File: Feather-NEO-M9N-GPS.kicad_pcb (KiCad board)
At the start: 2 copper layers, 50.8 x 22.9 mm, 43 parts, among them IC1 PRTR5V0U2F,115, J6 USB_B_Micro, U1 NEO-M9N

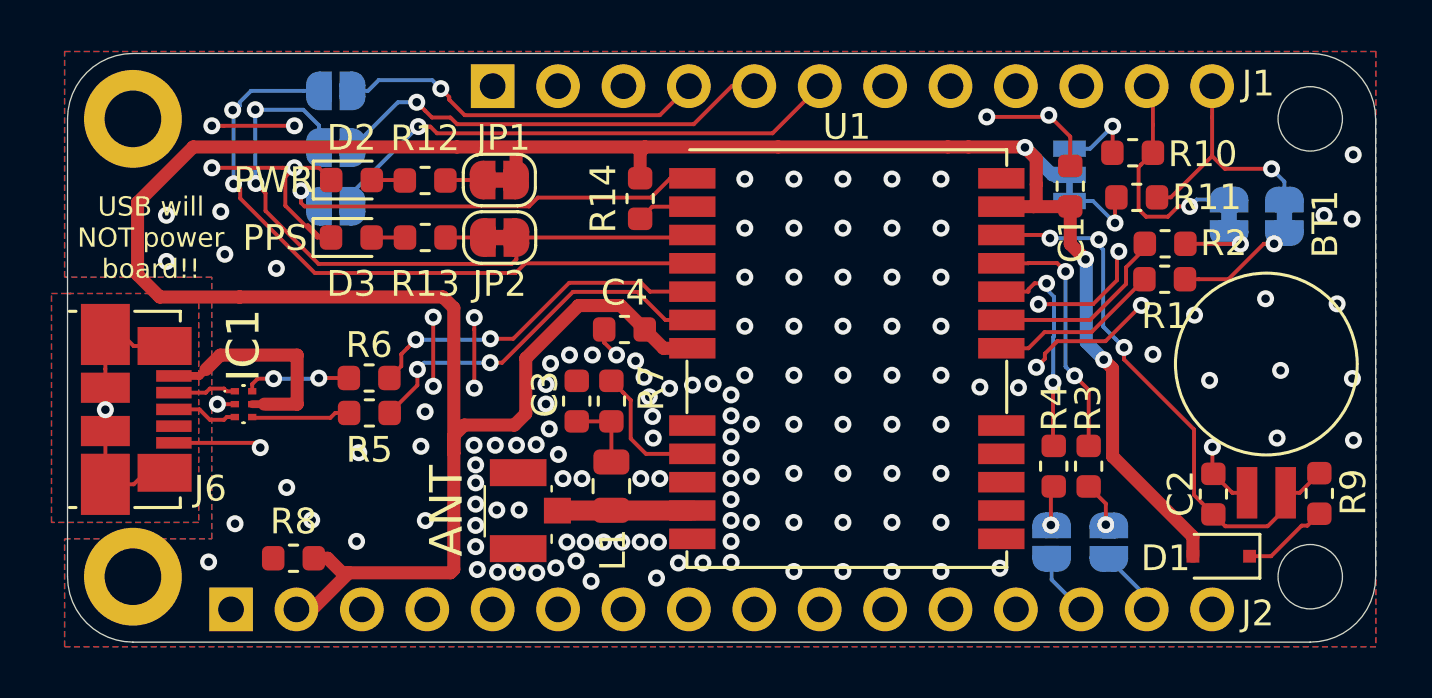
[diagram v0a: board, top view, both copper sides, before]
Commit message: Rev2!
Rev2 includes proper USB implementation, some small trace fixes, and power regulation
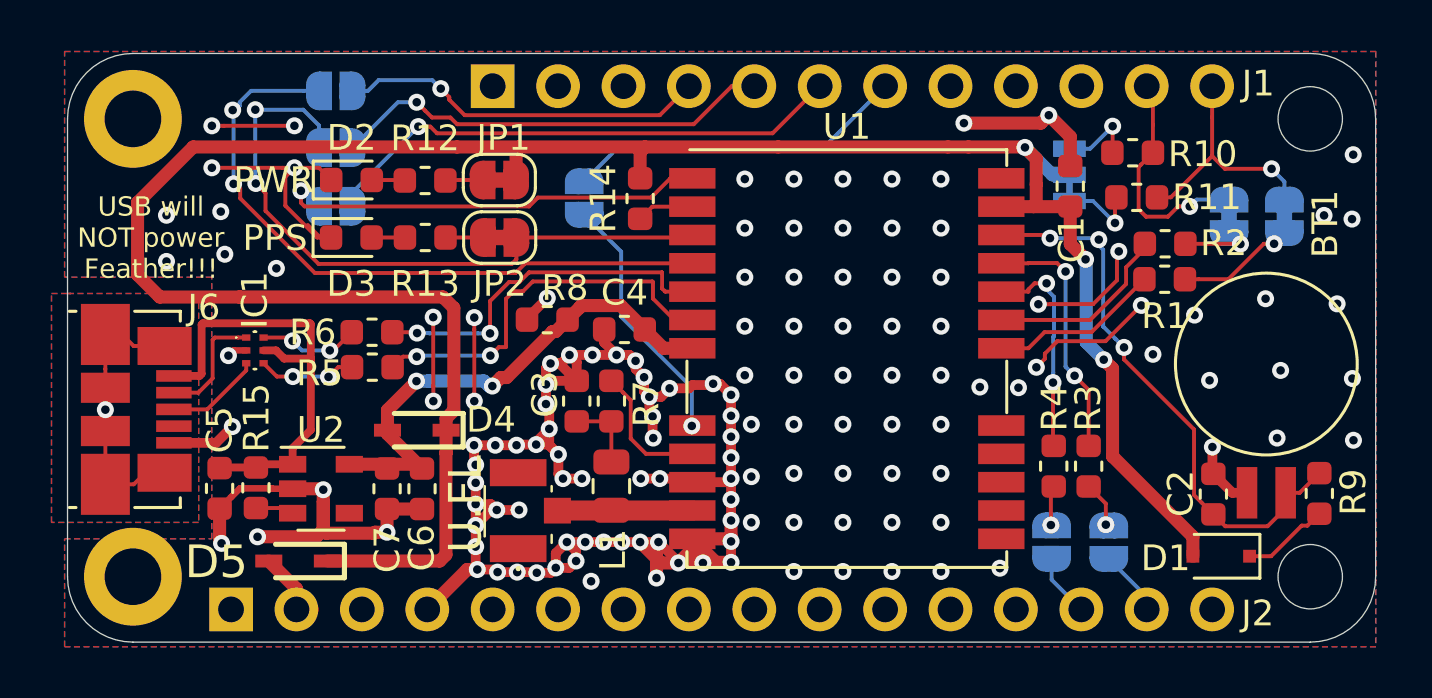
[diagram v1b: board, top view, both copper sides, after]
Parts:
- added C5: 10uF, Capacitor_SMD:C_0603_1608Metric, F.Cu at (134.5, 91.4)
- added C6: 10uF, Capacitor_SMD:C_0603_1608Metric, F.Cu at (142.4, 91.4)
- added C7: 1uF, Capacitor_SMD:C_0603_1608Metric, F.Cu at (141.0, 91.4)
- added D4: BAT60AE6327HTSA1, SamacSys_Parts:SOD2513X110N, F.Cu at (142.2, 89.1)
- added D5: BAT60AE6327HTSA1, SamacSys_Parts:SOD2513X110N, F.Cu at (137.6, 94.2)
- added JP5: ~RESET_GPS, Jumper:SolderJumper-2_P1.3mm_Open_RoundedPad1.0x1.5mm, B.Cu at (148.7, 80.1)
- added R15: 100k, Resistor_SMD:R_0603_1608Metric, F.Cu at (136.0, 91.4)
- added U2: AP2112K-3.3, Package_TO_SOT_SMD:SOT-23-5, F.Cu at (138.5, 91.4)
- ANT1: value ANT -> U.FL
- moved R8 13.5 mm to (147.3, 84.8)
- moved IC1 2.13 mm to (135.9, 86.0)
- moved R6 1.78 mm to (140.5, 85.3)
- moved R5 1.78 mm to (140.5, 86.7)
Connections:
- net Net-(IC1-Pad5) renamed +5V
- C4 pad 2: +3V3 -> /VDD_USB
- J2 pad 2: +3V3 -> Net-(D5-Pad2)
- R8 pad 2: +3V3 -> /VDD_USB
- U1 pad 7: +3V3 -> /VDD_USB
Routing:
- net GND: track 41.0 -> 127.7 mm, vias 146 -> 141
- net /VDD_USB: track 0.00 -> 20.1 mm, vias 0 -> 2
- net +3V3: track 109.0 -> 91.0 mm
- net /10`: track 0.00 -> 13.2 mm
- net /~RESET_GPS: track 0.00 -> 9.93 mm, vias 0 -> 1
- net +5V: track 8.77 -> 17.9 mm
- net Net-(D5-Pad2): track 0.00 -> 2.93 mm
- net Net-(IC1-Pad1): track 2.48 -> 4.58 mm
- net Net-(R15-Pad2): track 0.00 -> 1.51 mm
- net Net-(IC1-Pad3): track 2.58 -> 3.71 mm
- net Net-(R5-Pad1): track 14.5 -> 15.1 mm
- net /D+: track 3.85 -> 3.81 mm, vias 0 -> 2
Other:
- board text added: "10"
- board text added: "Rev2 ABW 1/6/20"
- board text added: "USB will NOT power Feather!!!"
- board text removed: "Rev1 ABW 12/26/19"
- board text removed: "USB will NOT power board!!"
